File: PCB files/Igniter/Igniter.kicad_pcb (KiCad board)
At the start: 2 copper layers, 124.9 x 69.6 mm, 56 parts, among them IC1 74HC4050, J1 PT, J10 SL3, J11 SL4, J12 SL5, J13 Micro_SD_Card, J2 PT, J3 PT, J4 PT, J5 Battery, J6 Ignition Coil +, J7 Ignition coil -, J8 SL1, J9 SL2, Q1 N MOSFET, Q2 N MOSFET, Q3 N MOSFET, Q4 N MOSFET, Q5 N MOSFET, Q6 N MOSFET, SW1 ARM, U2 FDS8984, U3 FDS8984, U4 FDS8984

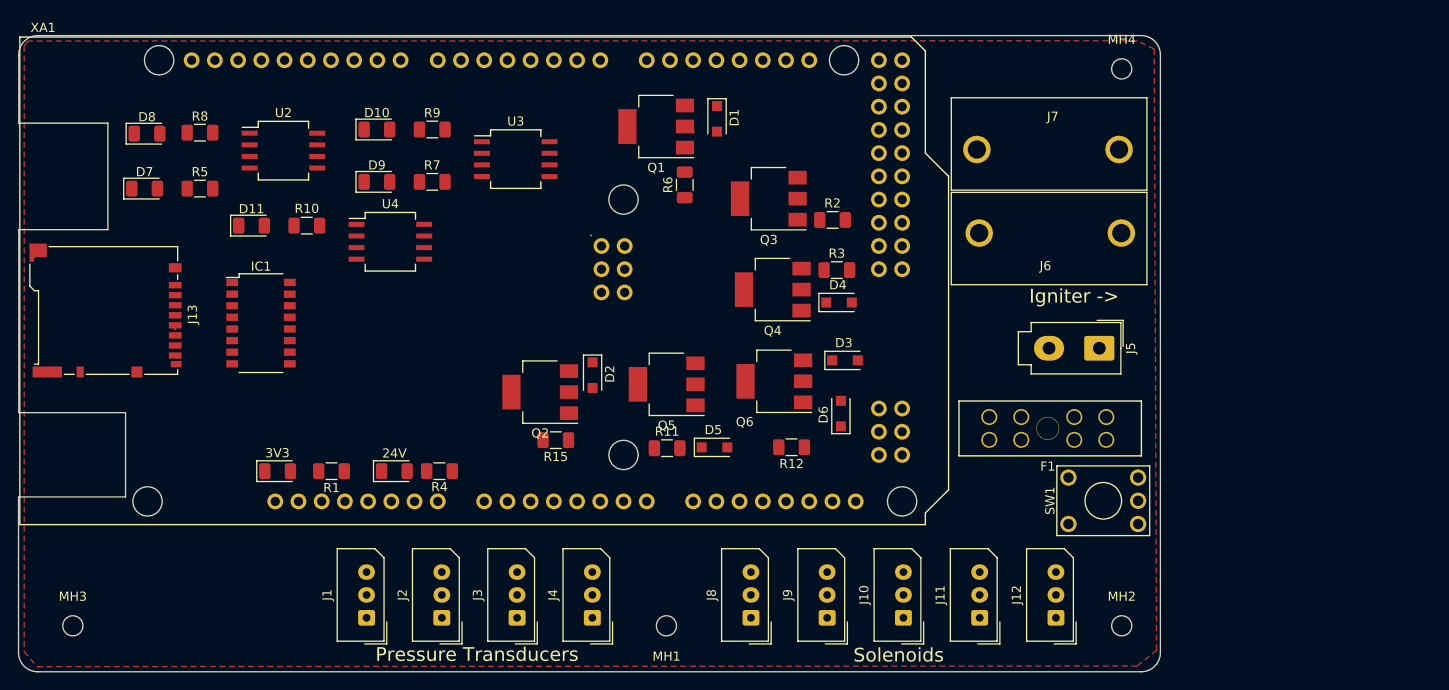
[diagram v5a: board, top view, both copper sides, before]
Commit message: 1/4/2020
Happy new year!
-Arranged parts on board to allocate space for power switch
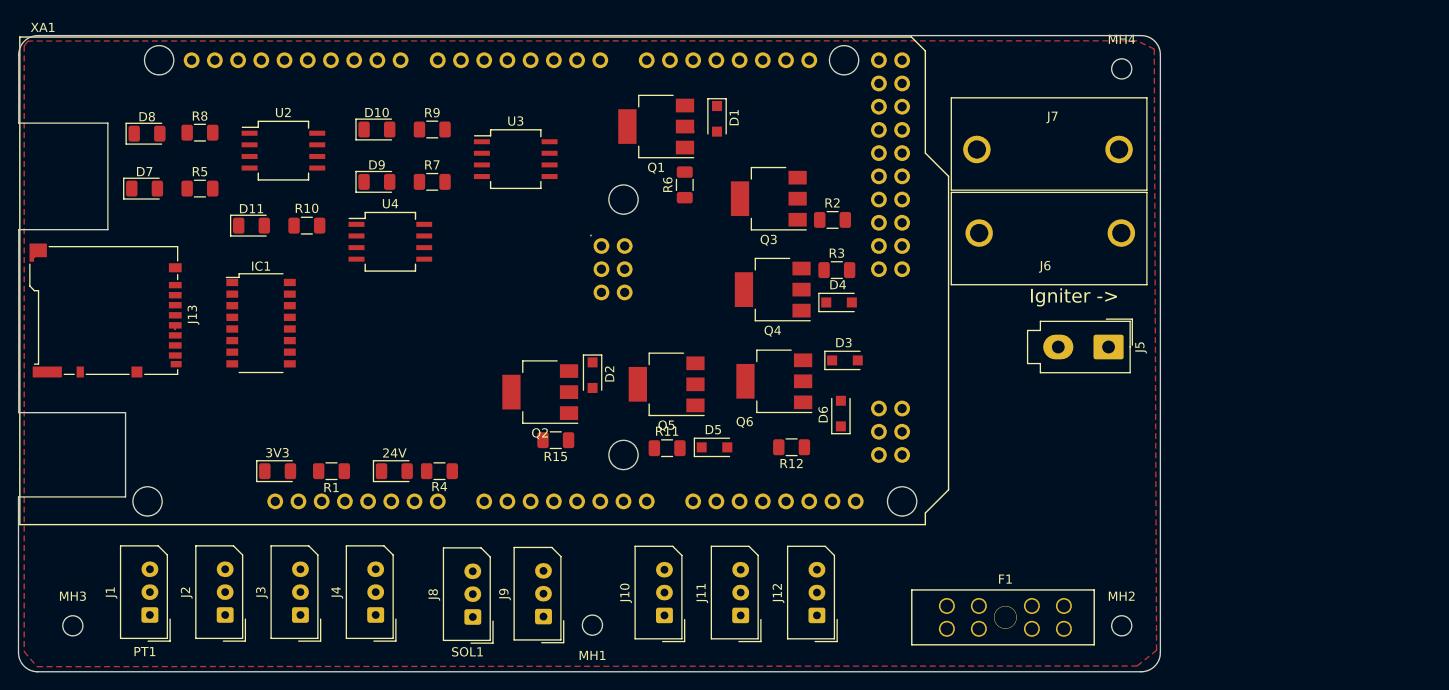
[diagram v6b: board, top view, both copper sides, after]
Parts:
- removed SW1: ARM, Button_Switch_THT:KSA_Tactile_SPST
- moved J9 31.0 mm to (142.5, 149.7)
- moved J8 30.4 mm to (134.8, 149.7)
- moved J11 26.1 mm to (164.1, 149.6)
- moved J10 26.1 mm to (155.8, 149.6)
- moved J12 26.1 mm to (172.4, 149.6)
- moved J2 23.7 mm to (107.7, 149.5)
- moved J1 23.7 mm to (99.5, 149.5)
- moved J3 23.7 mm to (115.9, 149.5)
- moved J4 23.7 mm to (124.2, 149.5)
- moved F1 21.2 mm to (193.1, 149.8), turned to 180 degrees
- moved MH1 8.10 mm to (147.9, 150.6)
- moved J5 1.02 mm to (204.3, 120.2)
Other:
- board text added: "PT1"
- board text added: "SOL1"
- board text removed: "Pressure Transducers"
- board text removed: "Solenoids"
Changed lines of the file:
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@@
   (general
     (thickness 1.6)
-    (drawings 26)
+    (drawings 28)
     (tracks 4)
     (zones 0)
-    (modules 56)
+    (modules 55)
     (nets 113)
   )
@@
   )
   (module Connector_Molex:Molex_SPOX_5267-03A_1x03_P2.50mm_Vertical (layer F.Cu)
-    (at 198.57974 149.8219 90)
+    (at 172.43552 149.56282 90)
     (descr "Molex SPOX Connector System, 5267-03A, 3 Pins per row (http://www.molex.com/pdm_docs/sd/022035035_sd.pdf), generated with kicad-footprint-generator")
     (tags "connector Molex SPOX side entry")
@@
   )
   (module Connector_Molex:Molex_SPOX_5267-03A_1x03_P2.50mm_Vertical (layer F.Cu)
-    (at 190.23838 149.8219 90)
+    (at 164.09416 149.56282 90)
     (descr "Molex SPOX Connector System, 5267-03A, 3 Pins per row (http://www.molex.com/pdm_docs/sd/022035035_sd.pdf), generated with kicad-footprint-generator")
     (tags "connector Molex SPOX side entry")
@@
   )
   (module Connector_Molex:Molex_SPOX_5267-03A_1x03_P2.50mm_Vertical (layer F.Cu)
-    (at 181.89702 149.8219 90)
+    (at 155.7528 149.56282 90)
     (descr "Molex SPOX Connector System, 5267-03A, 3 Pins per row (http://www.molex.com/pdm_docs/sd/022035035_sd.pdf), generated with kicad-footprint-generator")
     (tags "connector Molex SPOX side entry")
@@
   )
   (module Connector_Molex:Molex_SPOX_5267-03A_1x03_P2.50mm_Vertical (layer F.Cu)
-    (at 173.55566 149.8219 90)
+    (at 142.5194 149.68728 90)
     (descr "Molex SPOX Connector System, 5267-03A, 3 Pins per row (http://www.molex.com/pdm_docs/sd/022035035_sd.pdf), generated with kicad-footprint-generator")
     (tags "connector Molex SPOX side entry")
@@
   )
   (module Connector_Molex:Molex_SPOX_5267-03A_1x03_P2.50mm_Vertical (layer F.Cu)
-    (at 165.2143 149.8219 90)
+    (at 134.7851 149.73554 90)
     (descr "Molex SPOX Connector System, 5267-03A, 3 Pins per row (http://www.molex.com/pdm_docs/sd/022035035_sd.pdf), generated with kicad-footprint-generator")
     (tags "connector Molex SPOX side entry")
@@
   )
   (module IgniterCustom:FuseHolder (layer F.Cu)
-    (at 197.6882 129.1082)
+    (at 193.05202 149.77904 180)
     (fp_text reference F1 (at 0 4.1529) (layer F.SilkS)
       (effects (font (size 1 1) (thickness 0.15)))
@@
     (fp_line (start -9.7155 3) (end -9.7155 -3) (layer F.SilkS) (width 0.15))
     (fp_line (start 10.24128 3) (end 10.24128 -3) (layer F.SilkS) (width 0.15))
-    (pad "" np_thru_hole circle (at 0 0) (size 2.5 2.5) (drill 2.4) (layers *.Cu *.Mask))
-    (pad 1 thru_hole circle (at -6.4 -1.25 90) (size 1.75 1.75) (drill 1.4) (layers *.Cu *.Mask)
-      (net 6 +24V))
-    (pad 2 thru_hole circle (at -2.9 -1.25 90) (size 1.75 1.75) (drill 1.4) (layers *.Cu *.Mask)
-      (net 6 +24V))
-    (pad 5 thru_hole circle (at 2.9 -1.25 90) (size 1.75 1.75) (drill 1.4) (layers *.Cu *.Mask)
+    (pad "" np_thru_hole circle (at 0 0 180) (size 2.5 2.5) (drill 2.4) (layers *.Cu *.Mask))
+    (pad 1 thru_hole circle (at -6.4 -1.25 270) (size 1.75 1.75) (drill 1.4) (layers *.Cu *.Mask)
+      (net 6 +24V))
+    (pad 2 thru_hole circle (at -2.9 -1.25 270) (size 1.75 1.75) (drill 1.4) (layers *.Cu *.Mask)
+      (net 6 +24V))
+    (pad 5 thru_hole circle (at 2.9 -1.25 270) (size 1.75 1.75) (drill 1.4) (layers *.Cu *.Mask)
       (net 24 "Net-(F1-Pad5)"))
-    (pad 6 thru_hole circle (at 6.4 -1.25 90) (size 1.75 1.75) (drill 1.4) (layers *.Cu *.Mask)
+    (pad 6 thru_hole circle (at 6.4 -1.25 270) (size 1.75 1.75) (drill 1.4) (layers *.Cu *.Mask)
       (net 24 "Net-(F1-Pad5)"))
-    (pad 3 thru_hole circle (at -6.4 1.25 90) (size 1.75 1.75) (drill 1.4) (layers *.Cu *.Mask)
-      (net 6 +24V))
-    (pad 4 thru_hole circle (at -2.9 1.25 90) (size 1.75 1.75) (drill 1.4) (layers *.Cu *.Mask)
-      (net 6 +24V))
-    (pad 7 thru_hole circle (at 2.9 1.25 90) (size 1.75 1.75) (drill 1.4) (layers *.Cu *.Mask)
+    (pad 3 thru_hole circle (at -6.4 1.25 270) (size 1.75 1.75) (drill 1.4) (layers *.Cu *.Mask)
+      (net 6 +24V))
+    (pad 4 thru_hole circle (at -2.9 1.25 270) (size 1.75 1.75) (drill 1.4) (layers *.Cu *.Mask)
+      (net 6 +24V))
+    (pad 7 thru_hole circle (at 2.9 1.25 270) (size 1.75 1.75) (drill 1.4) (layers *.Cu *.Mask)
       (net 24 "Net-(F1-Pad5)"))
-    (pad 8 thru_hole circle (at 6.4 1.25 90) (size 1.75 1.75) (drill 1.4) (layers *.Cu *.Mask)
+    (pad 8 thru_hole circle (at 6.4 1.25 270) (size 1.75 1.75) (drill 1.4) (layers *.Cu *.Mask)
       (net 24 "Net-(F1-Pad5)"))
   )
@@
     )
   )
-  (module Button_Switch_THT:KSA_Tactile_SPST (layer F.Cu)
-    (at 199.9488 139.5603 90)
-    (descr "KSA http://www.ckswitches.com/media/1457/ksa_ksl.pdf")
-    (tags "SWITCH SMD KSA SW")
-    (fp_text reference SW1 (at 2.54 -2 90) (layer F.SilkS)
-      (effects (font (size 1 1) (thickness 0.15)))
-    )
-    (fp_text value ARM (at 2.54 10 90) (layer F.Fab)
-      (effects (font (size 1 1) (thickness 0.15)))
-    )
-    (fp_line (start -1.16 7.91) (end 6.24 7.91) (layer F.Fab) (width 0.1))
-    (fp_line (start 6.24 -0.29) (end -1.16 -0.29) (layer F.Fab) (width 0.1))
-    (fp_line (start -1.16 7.91) (end -1.16 -0.29) (layer F.Fab) (width 0.1))
-    (fp_text user %R (at 2.54 4 90) (layer F.Fab)
-      (effects (font (size 1 1) (thickness 0.15)))
-    )
-    (fp_line (start 6.35 8.89) (end 6.35 -1.27) (layer F.SilkS) (width 0.12))
-    (fp_line (start -1.27 -1.27) (end 6.35 -1.27) (layer F.SilkS) (width 0.12))
-    (fp_line (start -1.27 -1.27) (end -1.27 8.89) (layer F.SilkS) (width 0.12))
-    (fp_line (start -1.27 8.89) (end 6.35 8.89) (layer F.SilkS) (width 0.12))
-    (fp_line (start -1.41 -1.14) (end 6.49 -1.14) (layer F.CrtYd) (width 0.05))
-    (fp_line (start -1.41 -1.14) (end -1.41 8.75) (layer F.CrtYd) (width 0.05))
-    (fp_line (start 6.49 8.75) (end 6.49 -1.14) (layer F.CrtYd) (width 0.05))
-    (fp_line (start 6.49 8.75) (end -1.41 8.75) (layer F.CrtYd) (width 0.05))
-    (fp_circle (center 2.54 3.81) (end 0.54 3.81) (layer F.SilkS) (width 0.12))
-    (fp_line (start 6.24 7.91) (end 6.24 -0.29) (layer F.Fab) (width 0.1))
-    (pad 1 thru_hole circle (at 0 0 90) (size 1.778 1.778) (drill 1.143) (layers *.Cu *.Mask)
-      (net 109 "Net-(J5-Pad1)"))
-    (pad 2 thru_hole circle (at 5.08 0 90) (size 1.778 1.778) (drill 1.143) (layers *.Cu *.Mask)
-      (net 24 "Net-(F1-Pad5)"))
-    (pad 3 thru_hole circle (at 5.08 7.62 90) (size 1.778 1.778) (drill 1.143) (layers *.Cu *.Mask))
-    (pad 4 thru_hole circle (at 2.54 7.62 90) (size 1.778 1.778) (drill 1.143) (layers *.Cu *.Mask))
-    (pad 5 thru_hole circle (at 0 7.62 90) (size 1.778 1.778) (drill 1.143) (layers *.Cu *.Mask))
-    (model ${KISYS3DMOD}/Button_Switch_THT.3dshapes/KSA_Tactile_SPST.wrl
-      (at (xyz 0 0 0))
-      (scale (xyz 1 1 1))
-      (rotate (xyz 0 0 0))
-    )
-  )
   (module IgniterCustom:BananaJack15.5mm (layer F.Cu)
     (at 197.4343 107.7341)
@@
   )
   (module MountingHole:MountingHole_2.2mm_M2 (layer F.Cu)
-    (at 155.9687 150.6982)
+    (at 147.87372 150.62454)
     (descr "Mounting Hole 2.2mm, no annular, M2")
     (tags "mounting hole 2.2mm no annular m2")
@@
   )
   (module Connector_Molex:Molex_SPOX_5267-03A_1x03_P2.50mm_Vertical (layer F.Cu)
-    (at 123.1646 149.8219 90)
+    (at 99.46386 149.51456 90)
     (descr "Molex SPOX Connector System, 5267-03A, 3 Pins per row (http://www.molex.com/pdm_docs/sd/022035035_sd.pdf), generated with kicad-footprint-generator")
     (tags "connector Molex SPOX side entry")
@@
   )
   (module Connector_Molex:Molex_SPOX_5267-03A_1x03_P2.50mm_Vertical (layer F.Cu)
-    (at 131.398433 149.8219 90)
+    (at 107.697693 149.51456 90)
     (descr "Molex SPOX Connector System, 5267-03A, 3 Pins per row (http://www.molex.com/pdm_docs/sd/022035035_sd.pdf), generated with kicad-footprint-generator")
     (tags "connector Molex SPOX side entry")
@@
   )
   (module Connector_Molex:Molex_SPOX_5267-03A_1x03_P2.50mm_Vertical (layer F.Cu)
-    (at 139.632266 149.8219 90)
+    (at 115.931526 149.51456 90)
     (descr "Molex SPOX Connector System, 5267-03A, 3 Pins per row (http://www.molex.com/pdm_docs/sd/022035035_sd.pdf), generated with kicad-footprint-generator")
     (tags "connector Molex SPOX side entry")
@@
   )
   (module Connector_Molex:Molex_SPOX_5267-03A_1x03_P2.50mm_Vertical (layer F.Cu)
-    (at 147.8661 149.8219 90)
+    (at 124.16536 149.51456 90)
     (descr "Molex SPOX Connector System, 5267-03A, 3 Pins per row (http://www.molex.com/pdm_docs/sd/022035035_sd.pdf), generated with kicad-footprint-generator")
     (tags "connector Molex SPOX side entry")
@@
   )
   (module Connector_Molex:Molex_Mini-Fit_Jr_5566-02A_2x01_P4.20mm_Vertical (layer F.Cu)
-    (at 203.327 120.3325 270)
+    (at 204.33792 120.20042 270)
     (descr "Molex Mini-Fit Jr. Power Connectors, old mpn/engineering number: 5566-02A, example for new mpn: 39-28-x02x, 1 Pins per row, Mounting:  (http://www.molex.com/pdm_docs/sd/039281043_sd.pdf), generated with kicad-footprint-generator")
     (tags "connector Molex Mini-Fit_Jr side entry")
@@
     )
   )
+  (gr_text "PT1\n" (at 98.91268 153.55316) (layer F.SilkS)
+    (effects (font (size 1 1) (thickness 0.15)))
+  )
+  (gr_text SOL1 (at 134.21614 153.5811) (layer F.SilkS)
+    (effects (font (size 1 1) (thickness 0.15)))
+  )
+  (gr_line (start 188.82868 124.23902) (end 203.31938 124.23902) (layer Dwgs.User) (width 0.15))
+  (gr_line (start 188.82868 144.95272) (end 188.82868 124.23902) (layer Dwgs.User) (width 0.15))
   (gr_text "Check diameter" (at 244.53342 150.71598) (layer Dwgs.User)
     (effects (font (size 1 1) (thickness 0.15)))
@@
     (effects (font (size 1.5 1.5) (thickness 0.3)))
   )
-  (gr_text Solenoids (at 181.37378 153.90876) (layer F.SilkS)
-    (effects (font (size 1.5 1.5) (thickness 0.3)))
-  )
-  (gr_text "Pressure Transducers" (at 135.24992 153.84018) (layer F.SilkS)
-    (effects (font (size 1.5 1.5) (thickness 0.3)))
-  )

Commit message: 1/5/2020
-Fixed mounting hole size
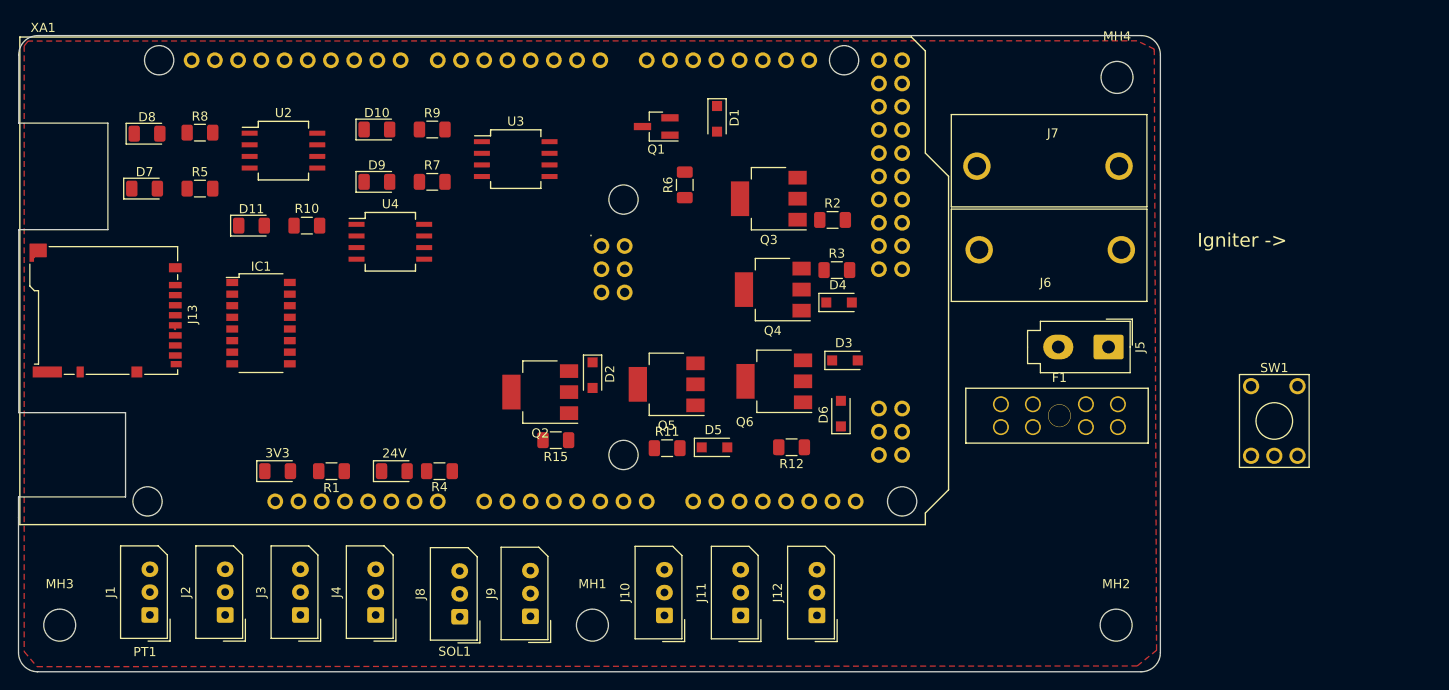
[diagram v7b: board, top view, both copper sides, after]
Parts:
- added SW1: ARM, Button_Switch_THT:KSA_Tactile_SPST, F.Cu at (219.9, 124.5)
- MH1, MH2, MH3, MH4: footprint MountingHole:MountingHole_2.2mm_M2 -> MountingHole:MountingHole_3.5mm
- Q1: footprint Package_TO_SOT_SMD:SOT-223 -> Package_TO_SOT_SMD:SOT-23_Handsoldering
- moved F1 22.8 mm to (199.0, 127.7)
- moved J6 1.83 mm to (197.4, 109.6)
- moved J7 1.83 mm to (198.2, 100.4)
- moved MH3 1.44 mm to (89.6, 150.6)
- moved J9 1.43 mm to (141.1, 149.7)
- moved J8 1.43 mm to (133.4, 149.7)
- moved MH4 1.06 mm to (205.3, 90.7)
- moved MH2 0.62 mm to (205.2, 150.6)
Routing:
- net Net-(D1-Pad2): track 1.34 -> 0.00 mm
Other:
- board text removed: "Check diameter"
